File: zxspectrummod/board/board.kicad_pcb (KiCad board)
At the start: 2 copper layers, 50.8 x 20.3 mm, 7 parts, among them IC1 LVC245A, IC2 LVC245A

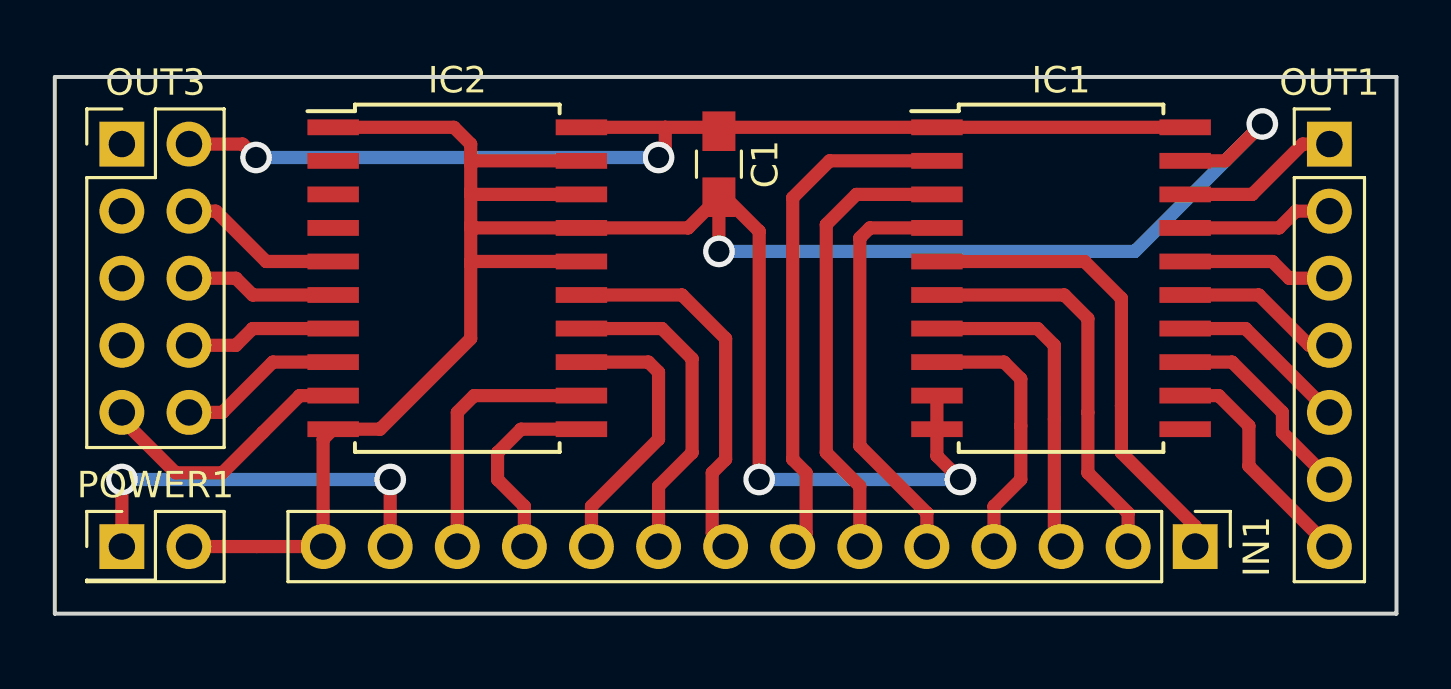
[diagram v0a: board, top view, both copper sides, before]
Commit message: small additions for zx spectrum mod
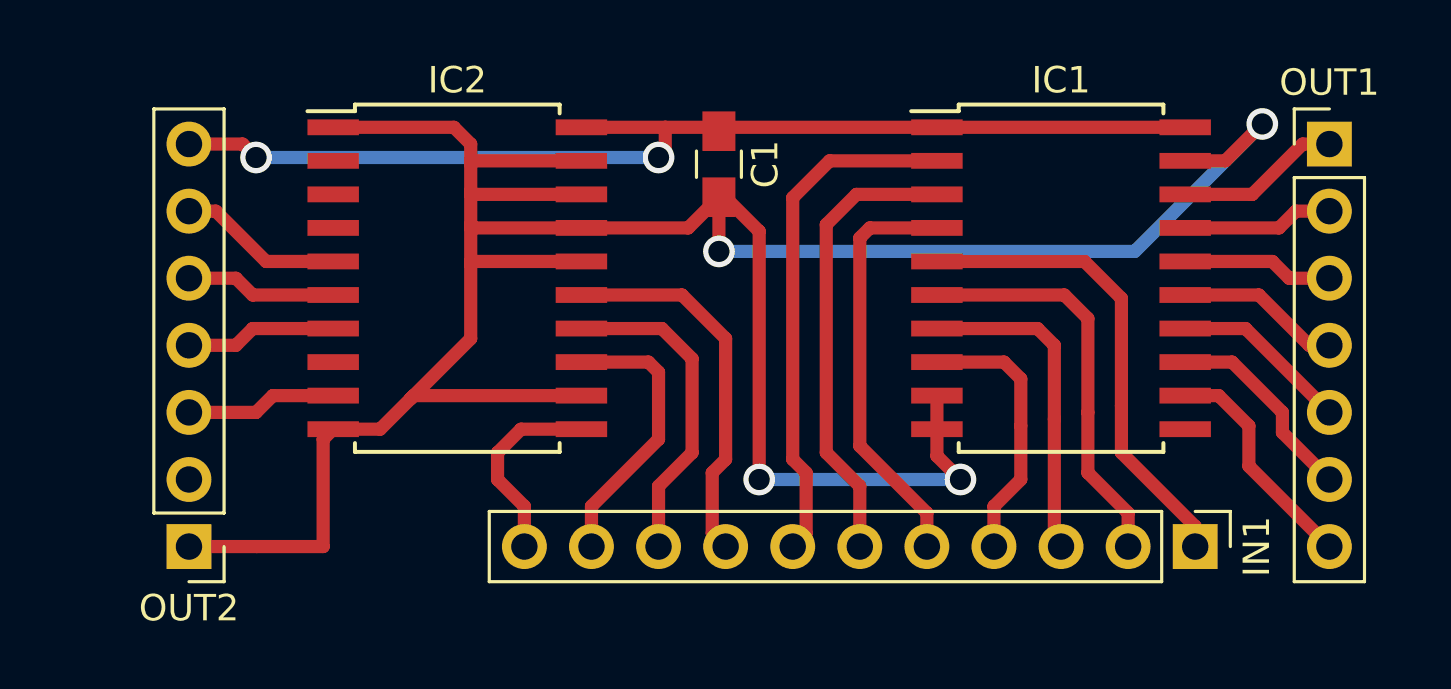
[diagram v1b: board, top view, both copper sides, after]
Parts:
- removed OUT3: CONN_02X05, Pin_Headers:Pin_Header_Straight_2x05_Pitch2.54mm
- removed POWER1: CONN_02X01, Pin_Headers:Pin_Header_Straight_2x01_Pitch2.54mm
- added OUT2: CONN_01X07, Pin_Headers:Pin_Header_Straight_1x07_Pitch2.54mm, F.Cu at (142.2, 109.2)
- IN1: value CONN_01X14 -> CONN_01X11; footprint Pin_Headers:Pin_Header_Straight_1x14_Pitch2.54mm -> Pin_Headers:Pin_Header_Straight_1x11_Pitch2.54mm
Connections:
- IC1 pad 2: /D2 -> /D3
- IC1 pad 3: /D1 -> /D2
- IC1 pad 4: /D0 -> /D1
- IC1 pad 8: /A0 -> /D0
- IC2 pad 11: /D6 -> /D7
- IC2 pad 12: /D7 -> GND
- IC2 pad 13: /D5 -> /D6
- IC2 pad 14: /D4 -> /D5
- IC2 pad 15: /D3 -> /D4
- IC2 pad 8: Net-(IC2-Pad8) -> (no net)
- IN1 pad 10: /D5 -> /D6
- IN1 pad 11: /D6 -> /D7
- IN1 pad 4: /A0 -> /D0
- IN1 pad 5: /D0 -> /D1
- IN1 pad 6: /D1 -> /D2
- IN1 pad 7: /D2 -> /D3
- IN1 pad 8: /D3 -> /D4
- IN1 pad 9: /D4 -> /D5
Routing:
- net +5V: track 15.2 -> 0.00 mm, vias 2 -> 0
- net /A0: track 10.2 -> 0.00 mm
- net GND: track 102.7 -> 109.3 mm
- net Net-(IC2-Pad8): track 6.25 -> 0.00 mm
- net /D0: track 15.8 -> 10.2 mm
- net /D3: track 14.4 -> 19.7 mm
- net Net-(IC2-Pad9): track 10.3 -> 5.72 mm
- net /D6: track 7.52 -> 10.7 mm
- net /D7: track 10.0 -> 7.52 mm
- net /D2: track 19.7 -> 17.4 mm
- net /D4: track 12.3 -> 14.4 mm
- net /D1: track 17.4 -> 15.8 mm
- net /D5: track 10.7 -> 12.3 mm
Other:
- board outline removed

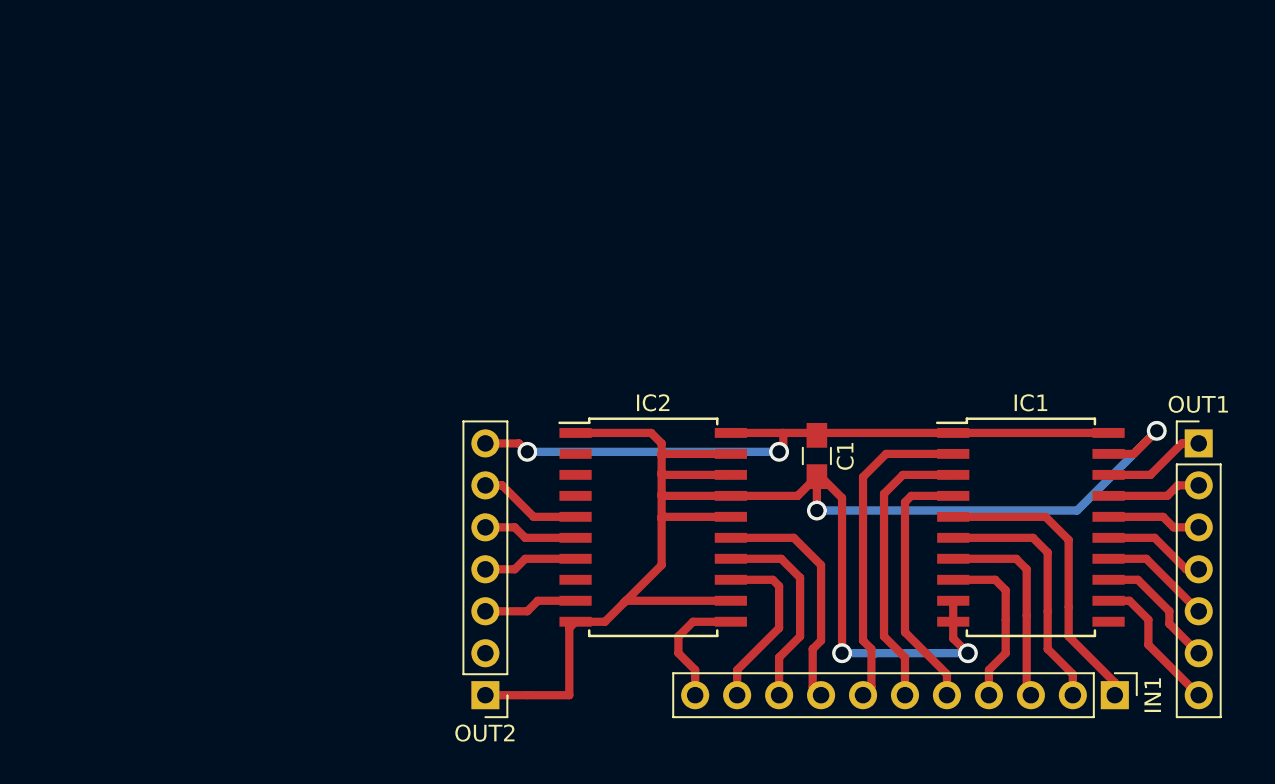
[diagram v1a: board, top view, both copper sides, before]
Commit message: Redesign ZX Spectrum Mod
To match the Rev.2 A-Video board
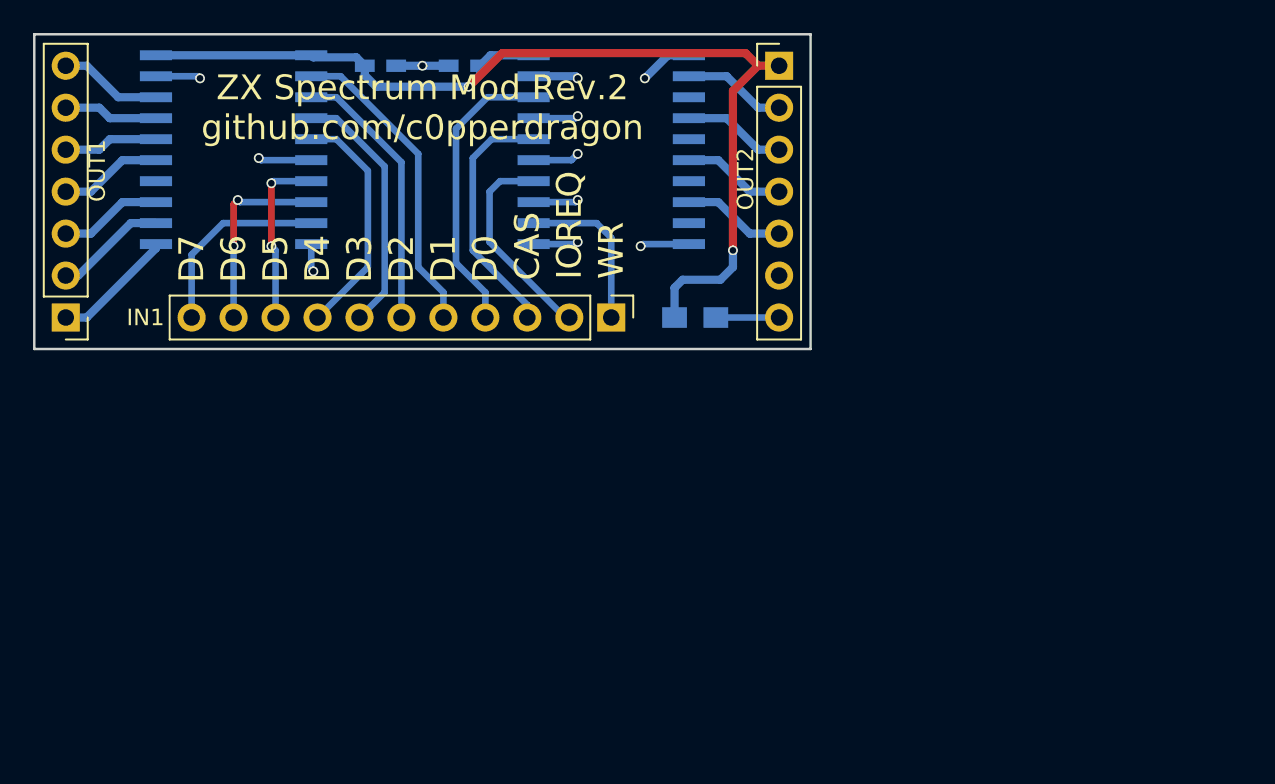
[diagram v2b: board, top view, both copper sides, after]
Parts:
- added C2: 100nF, Capacitors_SMD:C_0603_HandSoldering, B.Cu at (135.9, 71.1)
- added C3: 100nF, Capacitors_SMD:C_0603_HandSoldering, B.Cu at (141.0, 71.1)
- C1, IC1, IC2: moved to B.Cu
- moved OUT1 69.0 mm to (116.8, 86.4), turned to 180 degrees
- moved IC1 53.4 mm to (127.0, 76.2), turned to 180 degrees
- moved OUT2 42.0 mm to (160.0, 71.1), turned to 0 degrees
- moved IN1 38.1 mm to (149.9, 86.4)
- moved IC2 23.0 mm to (149.9, 76.2), turned to 180 degrees
- moved C1 11.2 mm to (154.9, 86.4), turned to 0 degrees
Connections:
- IC1 pad 11: (no net) -> Net-(IC1-Pad11)
- IC1 pad 14: Net-(IC1-Pad14) -> (no net)
- IC1 pad 2: /D3 -> /D1
- IC1 pad 4: /D1 -> /D3
- IC1 pad 5: /WR -> /D4
- IC1 pad 6: /IOREQ -> GND
- IC1 pad 7: /CAS -> /D5
- IC1 pad 8: /D0 -> /D6
- IC1 pad 9: GND -> /D7
- IC2 pad 11: /D7 -> GND
- IC2 pad 12: GND -> /WR
- IC2 pad 13: /D6 -> GND
- IC2 pad 14: /D5 -> /IOREQ
- IC2 pad 15: /D4 -> GND
- IC2 pad 16: GND -> /CAS
- IC2 pad 18: GND -> /D0
- IC2 pad 2: (no net) -> Net-(IC2-Pad2)
- IC2 pad 4: (no net) -> Net-(IC2-Pad4)
- IC2 pad 5: Net-(IC2-Pad5) -> (no net)
- IC2 pad 7: Net-(IC2-Pad7) -> (no net)
- IC2 pad 8: (no net) -> Net-(IC2-Pad8)
- IC2 pad 9: Net-(IC2-Pad9) -> (no net)
- OUT1 pad 1: Net-(IC1-Pad18) -> Net-(IC1-Pad11)
- OUT1 pad 2: Net-(IC1-Pad17) -> Net-(IC1-Pad12)
- OUT1 pad 3: Net-(IC1-Pad16) -> Net-(IC1-Pad13)
- OUT1 pad 5: Net-(IC1-Pad14) -> Net-(IC1-Pad16)
- OUT1 pad 6: Net-(IC1-Pad13) -> Net-(IC1-Pad17)
- OUT1 pad 7: Net-(IC1-Pad12) -> Net-(IC1-Pad18)
- OUT2 pad 1: GND -> +3V3
- OUT2 pad 2: (no net) -> Net-(IC2-Pad2)
- OUT2 pad 3: Net-(IC2-Pad9) -> Net-(IC2-Pad4)
- OUT2 pad 4: Net-(IC2-Pad7) -> Net-(IC2-Pad6)
- OUT2 pad 5: Net-(IC2-Pad6) -> Net-(IC2-Pad8)
- OUT2 pad 6: Net-(IC2-Pad5) -> (no net)
- OUT2 pad 7: +3V3 -> GND
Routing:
- net GND: track 109.3 -> 34.6 mm, vias 4 -> 11
- net +3V3: track 42.2 -> 63.7 mm
- net /WR: track 18.1 -> 9.89 mm
- net Net-(IC1-Pad11): track 0.00 -> 7.45 mm
- net /D0: track 10.2 -> 17.7 mm
- net Net-(IC1-Pad14): track 6.78 -> 0.00 mm
- net Net-(IC2-Pad8): track 0.00 -> 6.25 mm
- net Net-(IC2-Pad4): track 0.00 -> 6.25 mm
- net Net-(IC2-Pad2): track 0.00 -> 6.25 mm
- net Net-(IC2-Pad5): track 6.25 -> 0.00 mm
- net Net-(IC2-Pad9): track 5.72 -> 0.00 mm
- net Net-(IC2-Pad7): track 5.72 -> 0.00 mm
- net /D7: track 7.52 -> 11.8 mm
- net /D3: track 19.7 -> 15.4 mm
- net /D1: track 15.8 -> 19.0 mm
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- added copper zone on F.Cu, net GND
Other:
- board outline added: 47 x 19 mm
- board text added: "CAS"
- board text added: "D0"
- board text added: "D1"
- board text added: "D2"
- board text added: "D3"
- board text added: "D4"
- board text added: "D5"
- board text added: "D6"
- board text added: "D7"
- board text added: "IOREQ"
- board text added: "WR"
- board text added: "ZX Spectrum Mod Rev.2 github.com/c0pperdragon"
